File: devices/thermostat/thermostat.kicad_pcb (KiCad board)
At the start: 2 copper layers, 90 x 107 mm, 44 parts, among them J1 1715721, J3 1715734, K1 SRD-05VDC-SL-C, K2 SRD-05VDC-SL-C, K3 SRD-05VDC-SL-C, SW1 PTS645SM43SMTR92 LFS, SW2 PTS645SM43SMTR92 LFS, SW3 PTS645SM43SMTR92 LFS, SW4 PTS645SM43SMTR92 LFS, SW5 PTS645SM43SMTR92 LFS, U1 ESP32-WROOM-32E-N4, U2 SHT40-AD1B-R3, U3 LM2596S-ADJ/NOPB, U4 AMS1117-3.3, U5 ULN2003AD

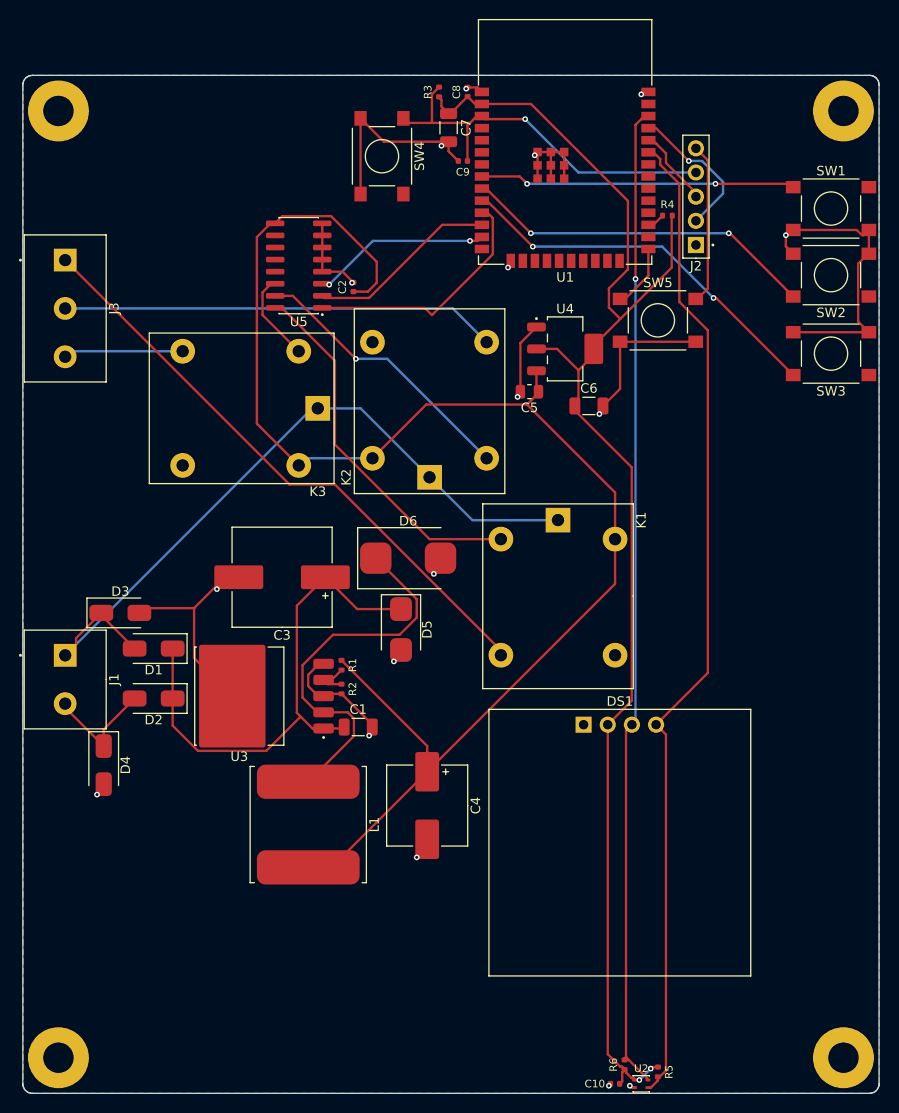
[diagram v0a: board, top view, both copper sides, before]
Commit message: devices: the thermostat's buck takes the TVS's clamp; p4-touch-7's host port is a Type-C source
- thermostat: the LM2596S-ADJ (45 V) sat under an SMBJ36A that clamps a surge near 58 V
  (rating-clamp). It is now the standard Buck block, which picks TI's LMR38020 (80 V) for the
  34 V rail; its 10 µF input capacitor is 1210 (CGA1210X5R106K630RT, 63 V). Placed again from
  scratch: 90 x 107 -> 84 x 76 mm. Up, down and mode stay on the right edge next to the OLED.
  Parts chosen from JLCPCB's catalogue. Complete: 0 errors, 1 warning (erc-rail-name).
- p4-touch-7: the USB host port J3 was a sink block (5.1 kΩ Rd on CC) with VBUS fed from VSYS
  through a Schottky. A device sees no source there. It is now pcbkit's new UsbCHost: 56 kΩ Rp on
  both CC pins to VSYS, and VBUS through an SY6280AAC limited to 750 mA (9.1 kΩ ISET). It stays on
  with the board: NucleoOS drives no enable pin. Complete: 0 errors; the router leaves two VSYS
  stubs (track-dangling warnings).

The MCU pins' nets are unchanged on both boards.

Claude-Session: https://claude.ai/code/session_01B3VRfBCg9vAvGVWujVGarr
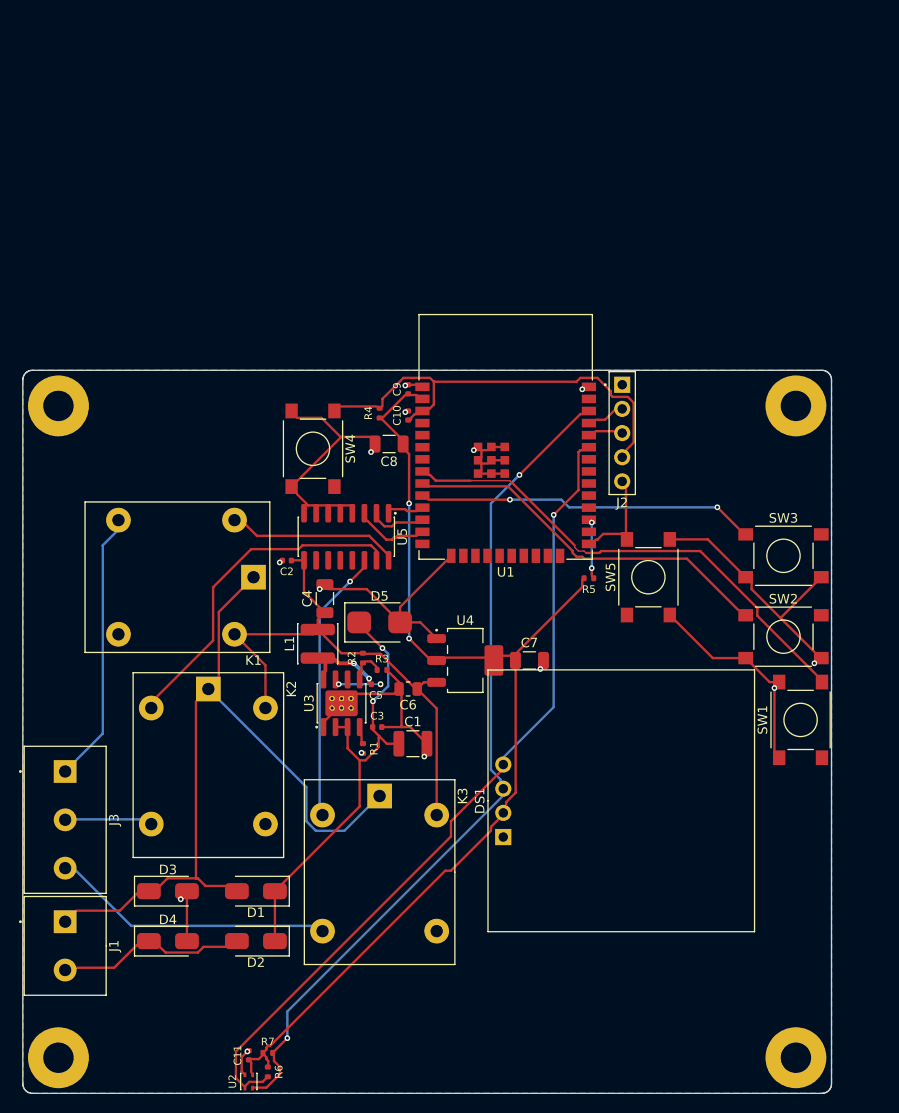
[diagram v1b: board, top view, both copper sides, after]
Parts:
- removed D6: schottky, D_SMC
- added C11: 100nF, C_0402_1005Metric, F.Cu at (123.8, 196.0)
- added R7: 10kohm, R_0402_1005Metric, F.Cu at (125.8, 195.8)
- C1: value 4.7uF -> 10uF; footprint C_1206_3216Metric -> C_1210_3225Metric
- C10: value 100nF -> 1uF
- C3: value 330uF -> 100nF; footprint CP_Elec_10x10 -> C_0402_1005Metric
- C4: value 220uF -> 22uF; footprint CP_Elec_8x10 -> C_1206_3216Metric
- C5: value 10uF -> 100nF; footprint C_0805_2012Metric -> C_0402_1005Metric
- C6: value 22uF -> 10uF; footprint C_1206_3216Metric -> C_0805_2012Metric
- C8: value 100nF -> 22uF; footprint C_0402_1005Metric -> C_1206_3216Metric
- C9: value 1uF -> 100nF
- H1, H2, H3, H4: value (none) -> MountingHole_3.2mm_M3_Pad
- J2: value (none) -> PinHeader_1x05_P2.54mm_Vertical
- L1: value 33uH -> 100uH; footprint L_Power_12x12mm -> L_Power_4x4mm
- R1: value 3.09kohm -> 52.3kohm
- R2: value 1kohm -> 120kohm
- R3: value 10kohm -> 30kohm
- U3: value LM2596S-ADJ/NOPB -> LMR38020SDDAR; footprint TO-263-5 -> SOIC-8-1EP_3.9x4.9mm_P1.27mm_EP2.71x3.4mm_ThermalVias
- moved C10 73.5 mm to (140.5, 128.8), turned to 90 degrees
- moved R3 61.0 mm to (137.8, 155.5), turned to 0 degrees
- moved C7 56.6 mm to (153.2, 154.5), turned to 0 degrees
- moved SW1 53.8 mm to (181.8, 160.8), turned to 270 degrees
- moved J3 53.8 mm to (104.5, 171.2)
- moved R5 52.4 mm to (159.5, 145.9), turned to 180 degrees
- moved K3 41.3 mm to (137.5, 168.8), turned to 270 degrees
- moved U2 41.3 mm to (123.8, 198.8), turned to 90 degrees
- moved SW2 38.3 mm to (179.9, 152.0), turned to 0 degrees
- moved C8 37.9 mm to (138.5, 131.8), turned to 180 degrees
- moved R6 37.5 mm to (125.8, 197.8), turned to 270 degrees
- moved R4 36.7 mm to (137.5, 128.5), turned to 90 degrees
- moved C6 35.3 mm to (140.5, 157.5), turned to 180 degrees
- moved C5 34.7 mm to (137.1, 157.0)
- moved U4 34.4 mm to (146.5, 154.5)
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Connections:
- C10 pad 1: V3 -> EN
- C5 pad 1: V5 -> buck/bst
- C5 pad 2: GND -> buck/sw
- C6 pad 1: V3 -> V5
- C9 pad 1: EN -> V3
- L1 pad 1: Net-(D6-1) -> buck/sw
- R1 pad 1: V5 -> buck/rt
- R1 pad 2: Net-(R1-2) -> GND
- R2 pad 1: Net-(R1-2) -> buck/fb
- R2 pad 2: GND -> V5
- R3 pad 1: V3 -> buck/fb
- R3 pad 2: EN -> GND
- R4 pad 1: Net-(R4-1) -> V3
- R4 pad 2: V3 -> EN
- R5 pad 1: V3 -> Net-(R5-1)
- R5 pad 2: SDA -> V3
- R6 pad 2: SCL -> SDA
- SW1 pad 2: UP -> GND
- SW2 pad 2: DOWN -> GND
- SW3 pad 2: MODE -> GND
- SW4 pad 2: EN -> GND
- SW5 pad 2: BOOT -> GND
- U1 pad 27: Net-(R4-1) -> Net-(R5-1)
- U3 pad 1: VDC -> GND
- U3 pad 2: Net-(D6-1) -> VDC
- U3 pad 3: GND -> VDC
- U3 pad 4: Net-(R1-2) -> buck/rt
- U3 pad 5: GND -> buck/fb
- U3 pad 6: GND -> (no net)
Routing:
- net V5: track 159.9 -> 57.3 mm
- net V3: track 145.4 -> 97.9 mm
- net Net-(D6-1): track 40.5 -> 0.00 mm
- net Y: track 45.8 -> 6.80 mm
- net W: track 63.3 -> 25.7 mm
- net HEAT: track 26.1 -> 2.88 mm
- net KW: track 38.9 -> 16.0 mm
- net SDA: track 105.0 -> 83.1 mm, vias 0 -> 1
- net SCL: track 104.2 -> 85.5 mm, vias 1 -> 2
- net KG: track 9.47 -> 26.7 mm, vias 0 -> 1
- net UP: track 33.2 -> 50.2 mm, vias 2 -> 0
- net BOOT: track 23.8 -> 7.65 mm
- net COOL: track 20.1 -> 4.41 mm
- net TX: track 15.5 -> 2.41 mm, vias 1 -> 0
- net G: track 14.2 -> 27.2 mm
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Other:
- board size 90 x 107 mm -> 85 x 76 mm

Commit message: registry: every board rebuilt with pcbkit main 4684674e6 - the bought part named on the board
pcbkit dc07fdfd6 writes the bought row's MPN and Manufacturer (the design's own kept as DesignMPN /
DesignManufacturer) and the build chooses parts before it places (6361ec104). Each of the 44 boards
was rebuilt (; the two P4 boards  only: their builds reroute pairs):
copper unchanged on all 44 (segments, arcs and vias counted before and after), placement kept; the
Arduino and lab boards now carry the parts the catalogue gives them. The check gains only the new
judgements: part-maker (a part bought from another maker) and part-missing on hand-fitted modules
(DS1 sockets); p4-touch-7 loses part-stale. The P4 boards keep their hole-clearance errors (a
reroute is Team 3's).

Claude-Session: https://claude.ai/code/session_01BAgp959tApA8aEg85EYgfb
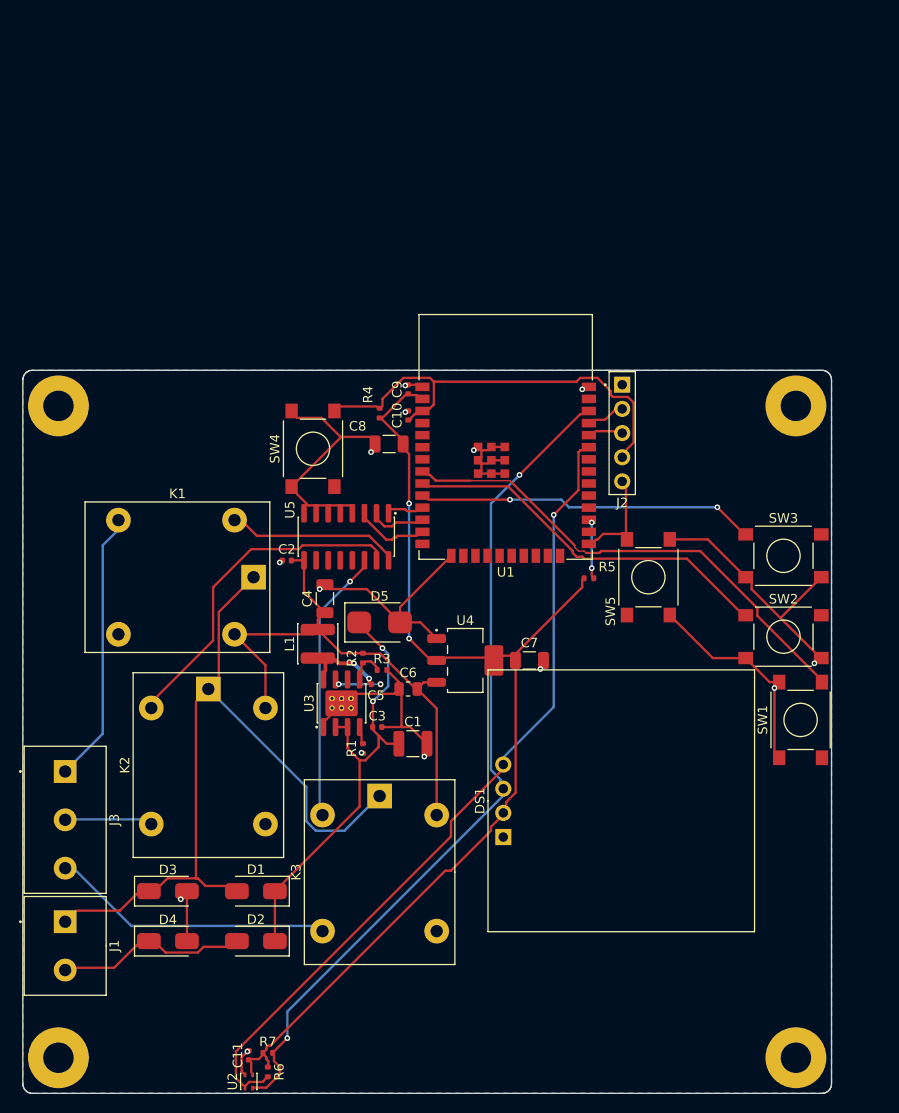
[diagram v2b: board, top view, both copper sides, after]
